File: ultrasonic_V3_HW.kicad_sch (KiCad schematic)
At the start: 0 parts

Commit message: schematics done
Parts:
- added J1: Conn_02x20_Odd_Even, symbol Connector_Generic:Conn_02x20_Odd_Even
- added J4: Conn_01x07_Pin, symbol Connector:Conn_01x07_Pin
- added J5: Screw_Terminal_01x02, symbol Connector:Screw_Terminal_01x02
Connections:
- new net CNTRL_CS: J1.24 (Pin_24)
- new net CNTRL_GPIO0: J1.19 (Pin_19)
- new net CNTRL_GPIO1: J1.21 (Pin_21)
- new net CNTRL_GPIO2: J1.23 (Pin_23)
- new net CNTRL_GPIO3: J1.25 (Pin_25)
- new net CNTRL_GPIO4: J1.27 (Pin_27)
- new net CNTRL_GPIO5: J1.29 (Pin_29)
- new net CNTRL_MISO: J1.22 (Pin_22)
- new net CNTRL_MOSI: J1.20 (Pin_20)
- new net CNTRL_SCLK: J1.26 (Pin_26)
- new net GND: J1.36 (Pin_36), J1.38 (Pin_38), J1.40 (Pin_40), J4.7 (Pin_7), J5.2 (Pin_2)
- new net JTAG_TCK: J4.2 (Pin_2)
- new net JTAG_TDI: J4.4 (Pin_4)
- new net JTAG_TDO: J4.3 (Pin_3)
- new net JTAG_TMS: J4.1 (Pin_1)
- new net LVDS_CS_N: J1.10 (Pin_10)
- new net LVDS_CS_P: J1.9 (Pin_9)
- new net LVDS_MISO_N: J1.6 (Pin_6)
- new net LVDS_MISO_P: J1.5 (Pin_5)
- new net LVDS_MOSI_N: J1.2 (Pin_2)
- new net LVDS_MOSI_P: J1.1 (Pin_1)
- new net LVDS_SCLK_N: J1.14 (Pin_14)
- new net LVDS_SCLK_P: J1.13 (Pin_13)
- new net P3V3: J4.6 (Pin_6)
- new net PowerManagement/P15V-20V_5S_UNREGULATED: J5.1 (Pin_1)
- no-connect marks 0 -> 1
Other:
- removed sheet BatteryManagement
- sheet AnalogFrontend ports: added ADC_D[0..9], ADC_INPUT, BRIDGE_B_signal, BRIDGE_D_signal, DAC_SPI, EN_SIGNAL_B, EN_SIGNAL_D, P3V3, P3V_REF, PGA_GATE2[0..4], PGA_GATE[0..4], STOP_SIGNAL; removed none
- sheet H-bridges ports: added BRIDGE_A_HI, BRIDGE_A_LO, BRIDGE_B_HI, BRIDGE_B_LO, BRIDGE_B_signal, BRIDGE_C_HI, BRIDGE_C_LO, BRIDGE_D_HI, BRIDGE_D_LO, BRIDGE_D_signal, P12V, PHV; removed none
- sheet PowerManagement ports: added EN_HV_REGULATOR, P12V, P15V-20V_5S_UNREGULATED, P3V3, P3V_REF, PGOOD_HV_REGULATOR, PHV; removed none
- sheet fpga ports: added ADC_D[0..9], ADC_INPUT, BRIDGE_A_HI, BRIDGE_A_LO, BRIDGE_B_HI, BRIDGE_B_LO, BRIDGE_C_HI, BRIDGE_C_LO, BRIDGE_D_HI, BRIDGE_D_LO, CNTRL_GPIO, CNTRL_SPI, DAC_SPI, EN_HV_REGULATOR, EN_SIGNAL_B, EN_SIGNAL_D, JTAG, LVDS, P3V3, PGA_GATE2[0..4], PGA_GATE[0..4], PGOOD_HV_REGULATOR, STOP_SIGNAL; removed none

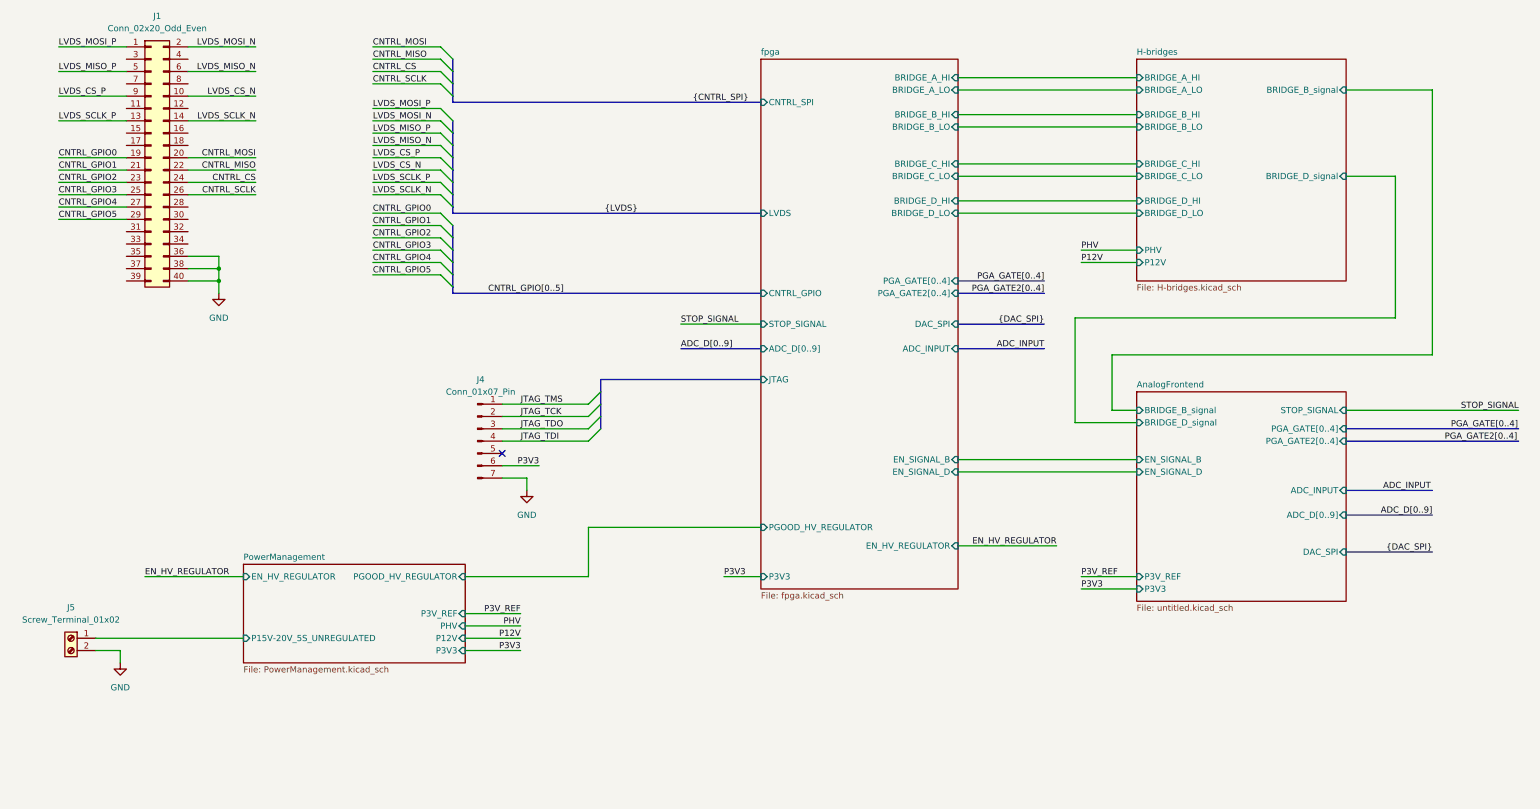
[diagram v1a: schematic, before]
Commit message: ready schematic for layout
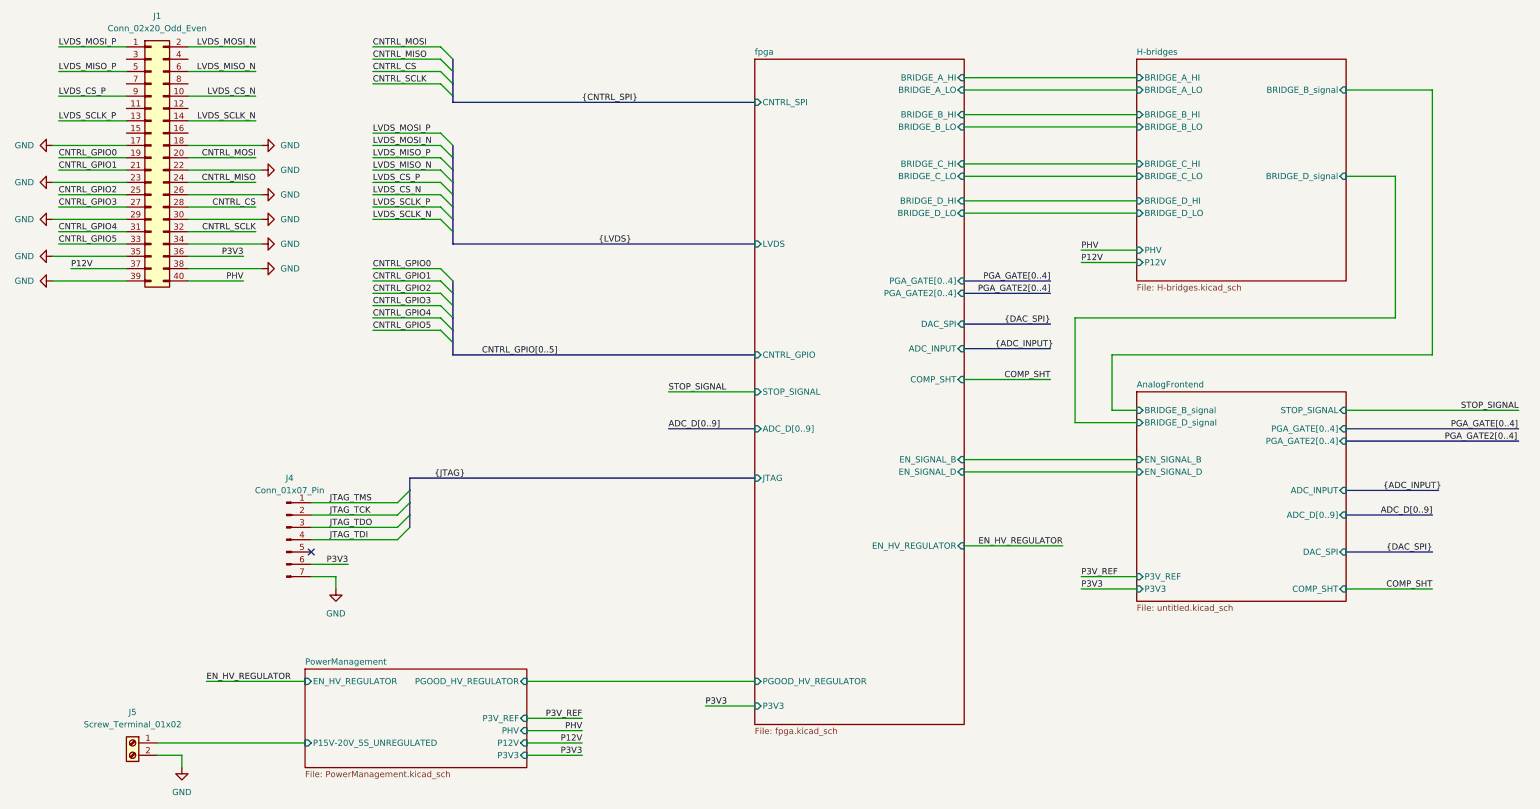
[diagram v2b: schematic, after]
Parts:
- J1: footprint (none) -> Connector_PinHeader_2.54mm:PinHeader_2x20_P2.54mm_Vertical
- J4: footprint (none) -> Connector_PinHeader_2.54mm:PinHeader_1x07_P2.54mm_Vertical
- J5: footprint (none) -> TerminalBlock_Phoenix:TerminalBlock_Phoenix_MKDS-1,5-2-5.08_1x02_P5.08mm_Horizontal
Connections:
- net CNTRL_CS: now also J1.28 (Pin_28); no longer J1.24 (Pin_24)
- net CNTRL_GPIO2: now also J1.25 (Pin_25); no longer J1.23 (Pin_23)
- net CNTRL_GPIO3: now also J1.27 (Pin_27); no longer J1.25 (Pin_25)
- net CNTRL_GPIO4: now also J1.31 (Pin_31); no longer J1.27 (Pin_27)
- net CNTRL_GPIO5: now also J1.33 (Pin_33); no longer J1.29 (Pin_29)
- net CNTRL_MISO: now also J1.24 (Pin_24); no longer J1.22 (Pin_22)
- net CNTRL_SCLK: now also J1.32 (Pin_32); no longer J1.26 (Pin_26)
- net GND: now also J1.17 (Pin_17), J1.18 (Pin_18), J1.22 (Pin_22), J1.23 (Pin_23), J1.26 (Pin_26), J1.29 (Pin_29), J1.30 (Pin_30), J1.34 (Pin_34), J1.35 (Pin_35), J1.39 (Pin_39); no longer J1.36 (Pin_36), J1.40 (Pin_40)
- net P12V: now also J1.37 (Pin_37)
- net P3V3: now also J1.36 (Pin_36)
- net PHV: now also J1.40 (Pin_40)
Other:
- sheet AnalogFrontend ports: added COMP_SHT; removed none
- sheet fpga ports: added COMP_SHT; removed none
- moved on the sheet: J4, J5

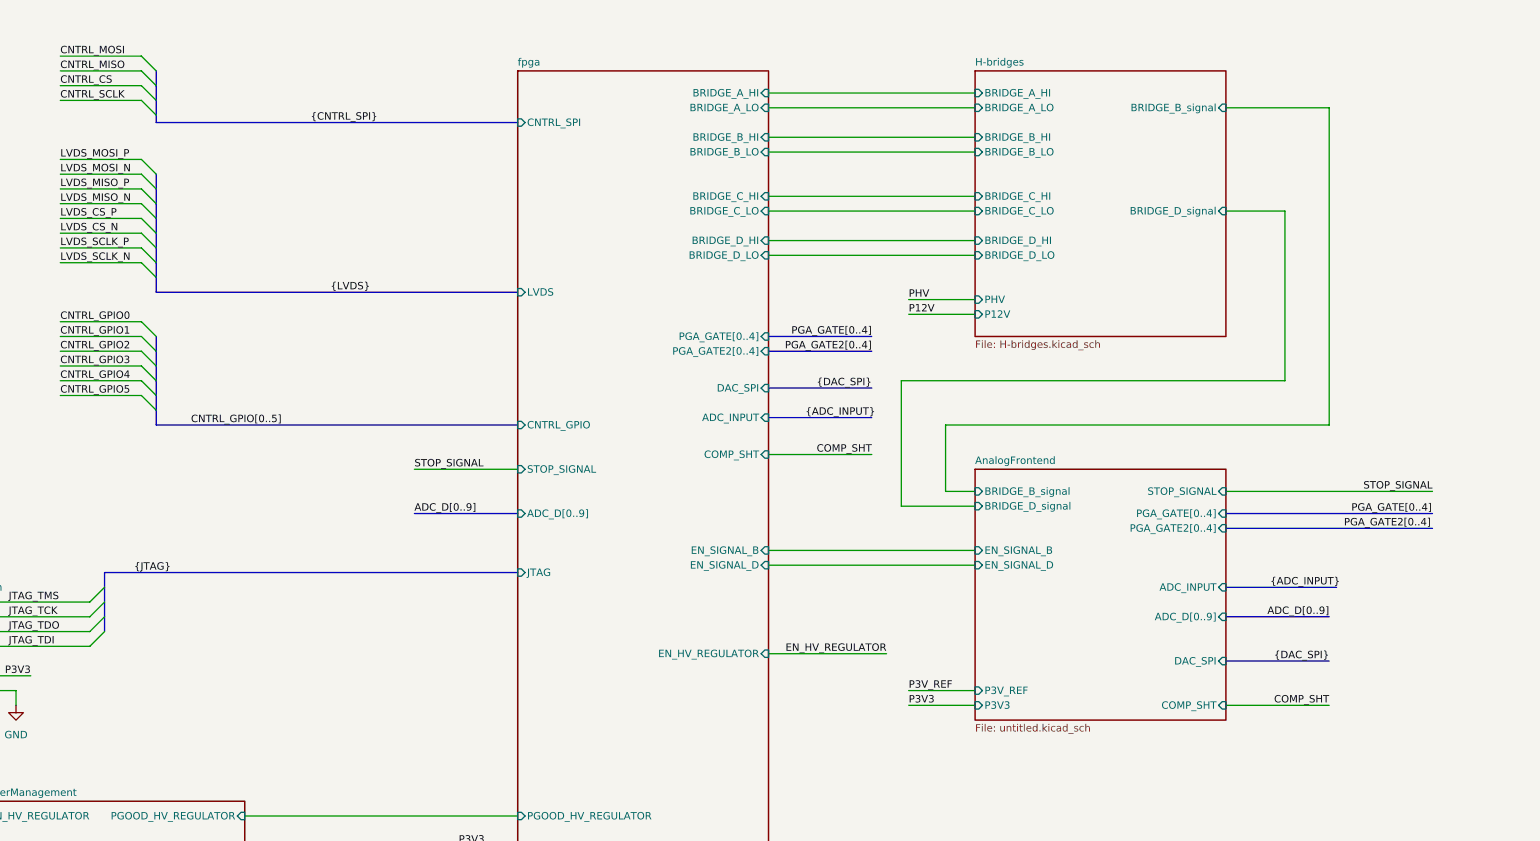
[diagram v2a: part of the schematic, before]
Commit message: new analog front end
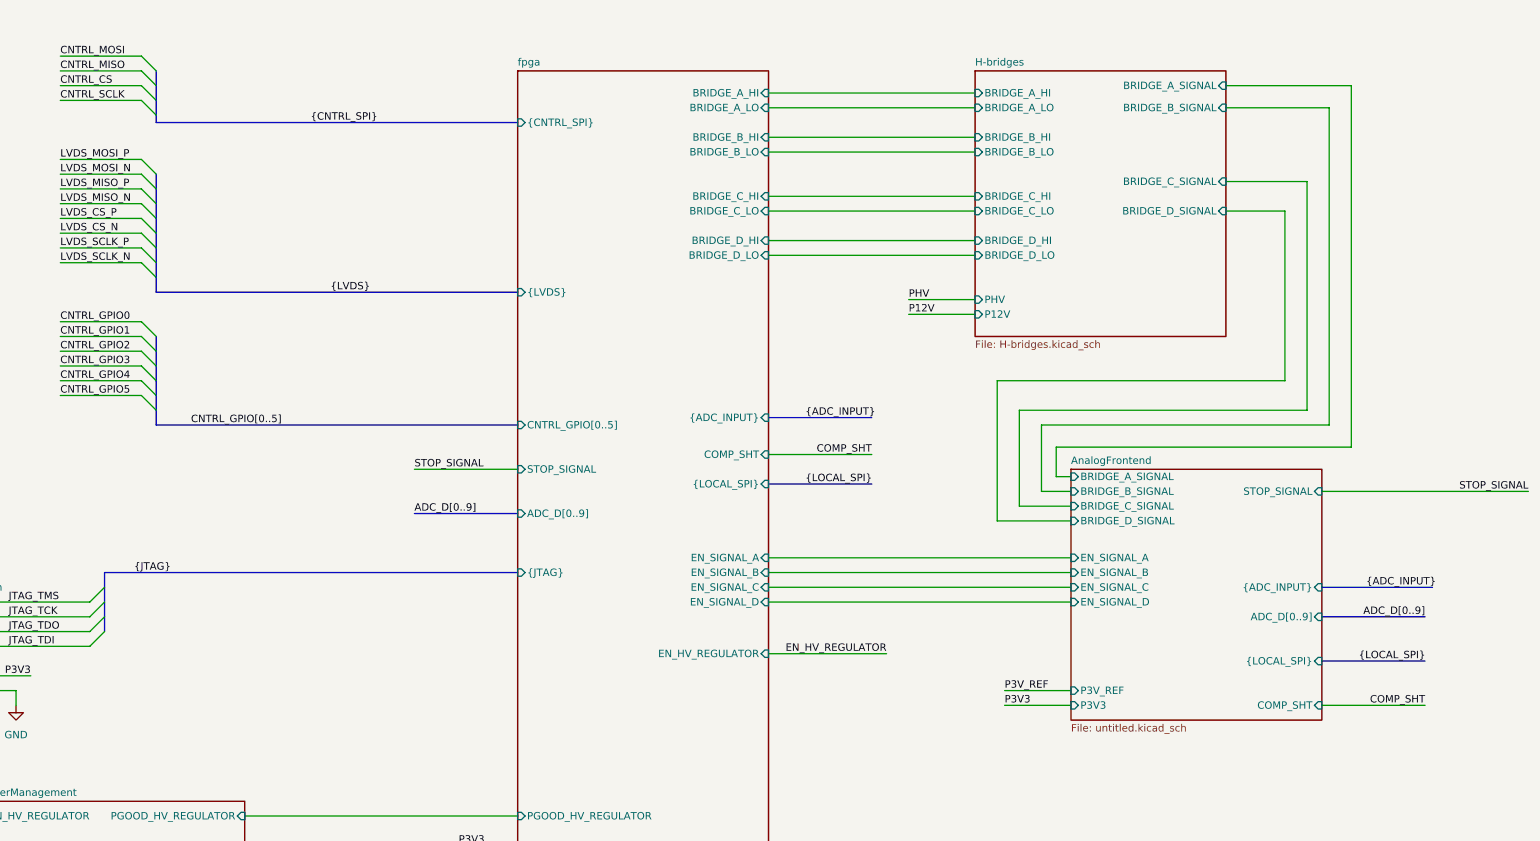
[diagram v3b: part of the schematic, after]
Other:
- sheet AnalogFrontend ports: added BRIDGE_A_SIGNAL, BRIDGE_B_SIGNAL, BRIDGE_C_SIGNAL, BRIDGE_D_SIGNAL, EN_SIGNAL_A, EN_SIGNAL_C, {ADC_INPUT}, {LOCAL_SPI}; removed ADC_INPUT, BRIDGE_B_signal, BRIDGE_D_signal, DAC_SPI, PGA_GATE2[0..4], PGA_GATE[0..4]
- sheet H-bridges ports: added BRIDGE_A_SIGNAL, BRIDGE_B_SIGNAL, BRIDGE_C_SIGNAL, BRIDGE_D_SIGNAL; removed BRIDGE_B_signal, BRIDGE_D_signal
- sheet fpga ports: added CNTRL_GPIO[0..5], EN_SIGNAL_A, EN_SIGNAL_C, {ADC_INPUT}, {CNTRL_SPI}, {JTAG}, {LOCAL_SPI}, {LVDS}; removed ADC_INPUT, CNTRL_GPIO, CNTRL_SPI, DAC_SPI, JTAG, LVDS, PGA_GATE2[0..4], PGA_GATE[0..4]

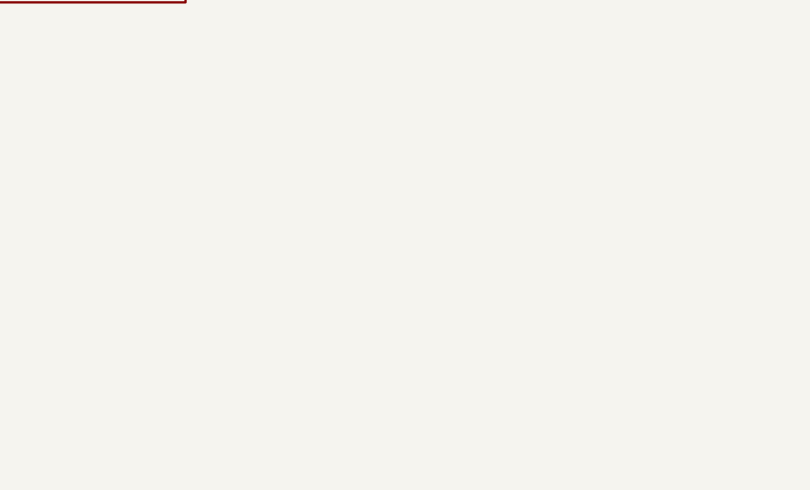
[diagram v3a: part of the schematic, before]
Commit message: schematic ready, basic layout done
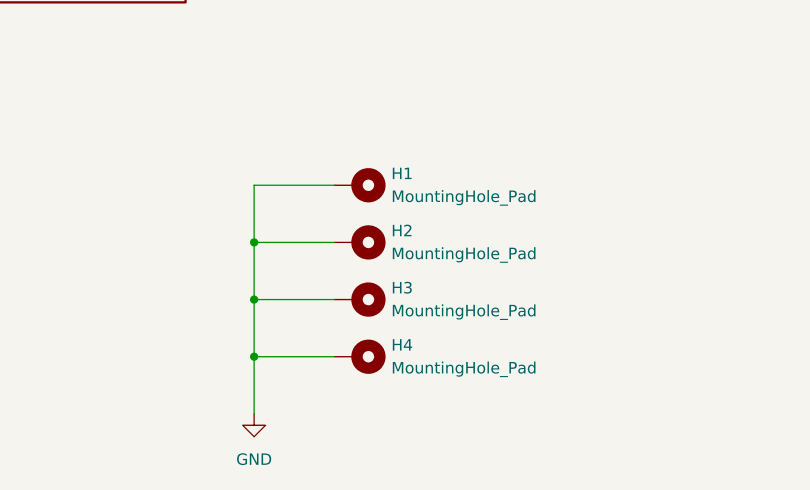
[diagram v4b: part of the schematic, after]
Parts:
- added H1, H2, H3, H4: MountingHole_Pad, MountingHole:MountingHole_3.2mm_M3_DIN965_Pad_TopBottom, symbol Mechanical:MountingHole_Pad
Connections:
- net GND: now also H1.1, H2.1, H3.1, H4.1
